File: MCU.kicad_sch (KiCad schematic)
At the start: 15 parts, among them U4 EFM32GG332, Y1 Crystal_GND23

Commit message: Added LED-s to mcu
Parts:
- added R18, R21, R22, R23, R24: 100, symbol Device:R
- added U11, U12: ~, symbol GuitarZero:LED_matrix
- C1: value 10µF -> 10u
- C1, C4: value 0.1µF -> 0.1u
- C1: value 10nF -> 10n
- C1: value 1µF -> 1u
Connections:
- net at U4.10 (PC1): now also U11.7 (C2)
- net at U4.11 (PC2): now also U11.8 (C3)
- net at U4.12 (PC3): now also U11.9 (C4)
- net at U4.13 (PC4): now also U11.10 (C5)
- net at U4.14 (PC5): now also U11.11 (C6)
- net at U4.15 (PB7): now also U11.12 (C7)
- net at U4.16 (PB8): now also R18.2
- net at U4.17 (PA8): now also R21.2
- net at U4.18 (PA9): now also R22.2
- net at U4.19 (PA10): now also R23.2
- net at U4.21 (PB11): now also R24.2
- net at U4.58 (PE9): now also U12.6 (C1)
- net at U4.59 (PE10): now also U12.7 (C2)
- net at U4.60 (PE11): now also U12.8 (C3)
- net at U4.61 (PE12): now also U12.9 (C4)
- net at U4.62 (PE13): now also U12.10 (C5)
- net at U4.63 (PE14): now also U12.11 (C6)
- net at U4.64 (PE15): now also U12.12 (C7)
- net at U4.9 (PC0): now also U11.6 (C1)
- new net: R24.1, U11.1 (R1), U12.1 (R1)
- new net: R21.1, U11.4 (R4), U12.4 (R4)
- new net: R23.1, U11.2 (R2), U12.2 (R2)
- new net: R22.1, U11.3 (R3), U12.3 (R3)
- new net: R18.1, U11.5 (R5), U12.5 (R5)
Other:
- moved on the sheet: C1

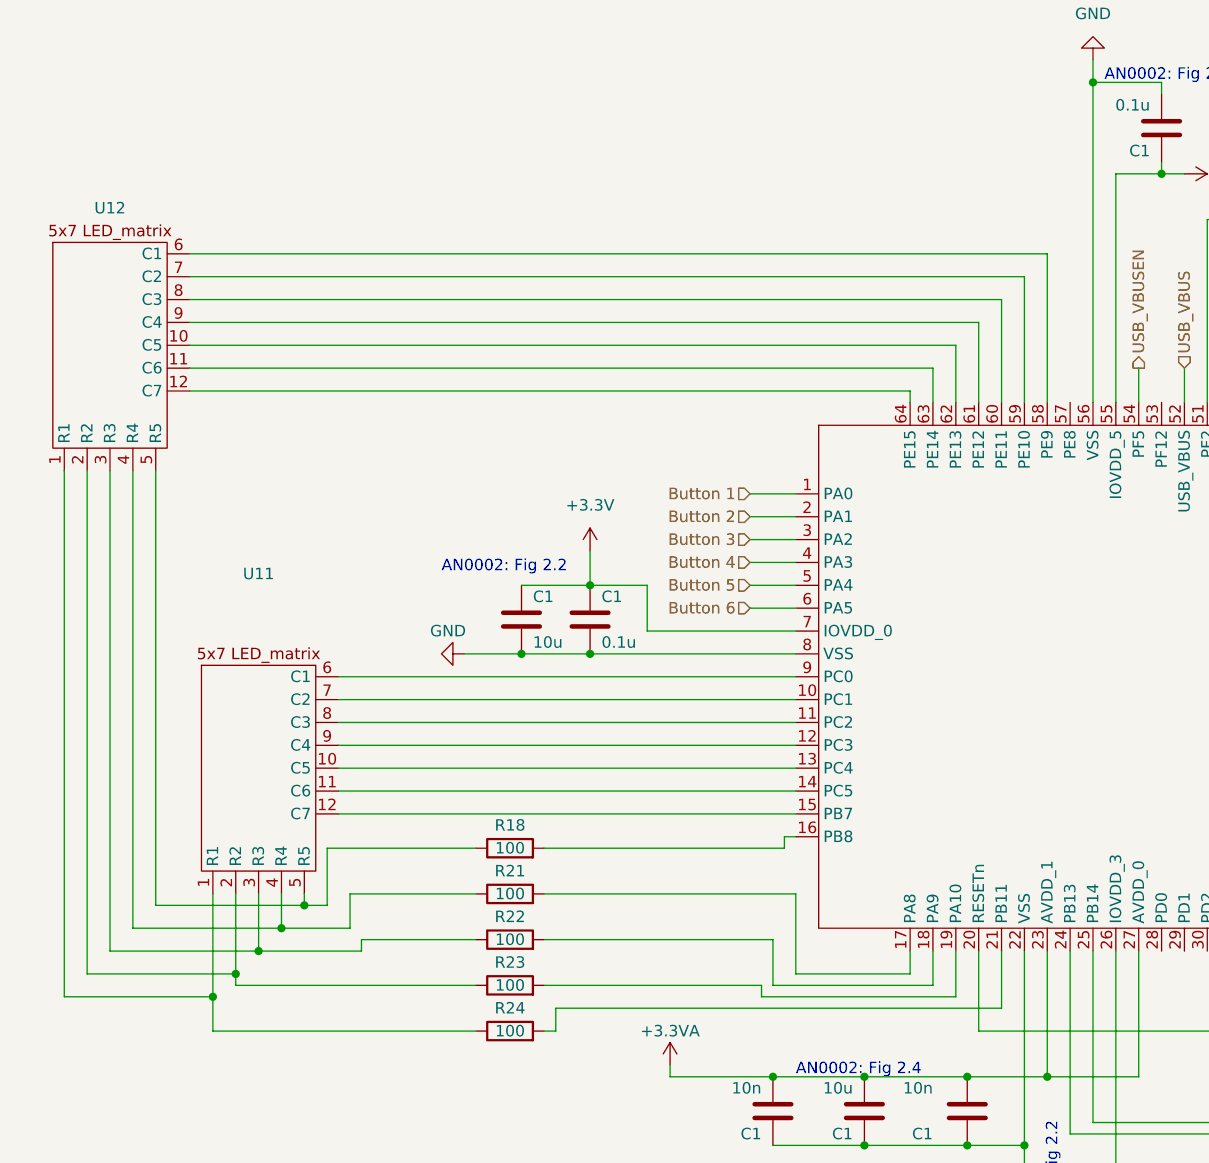
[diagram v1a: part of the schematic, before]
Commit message: Updated LEDs to match 14 pin layout
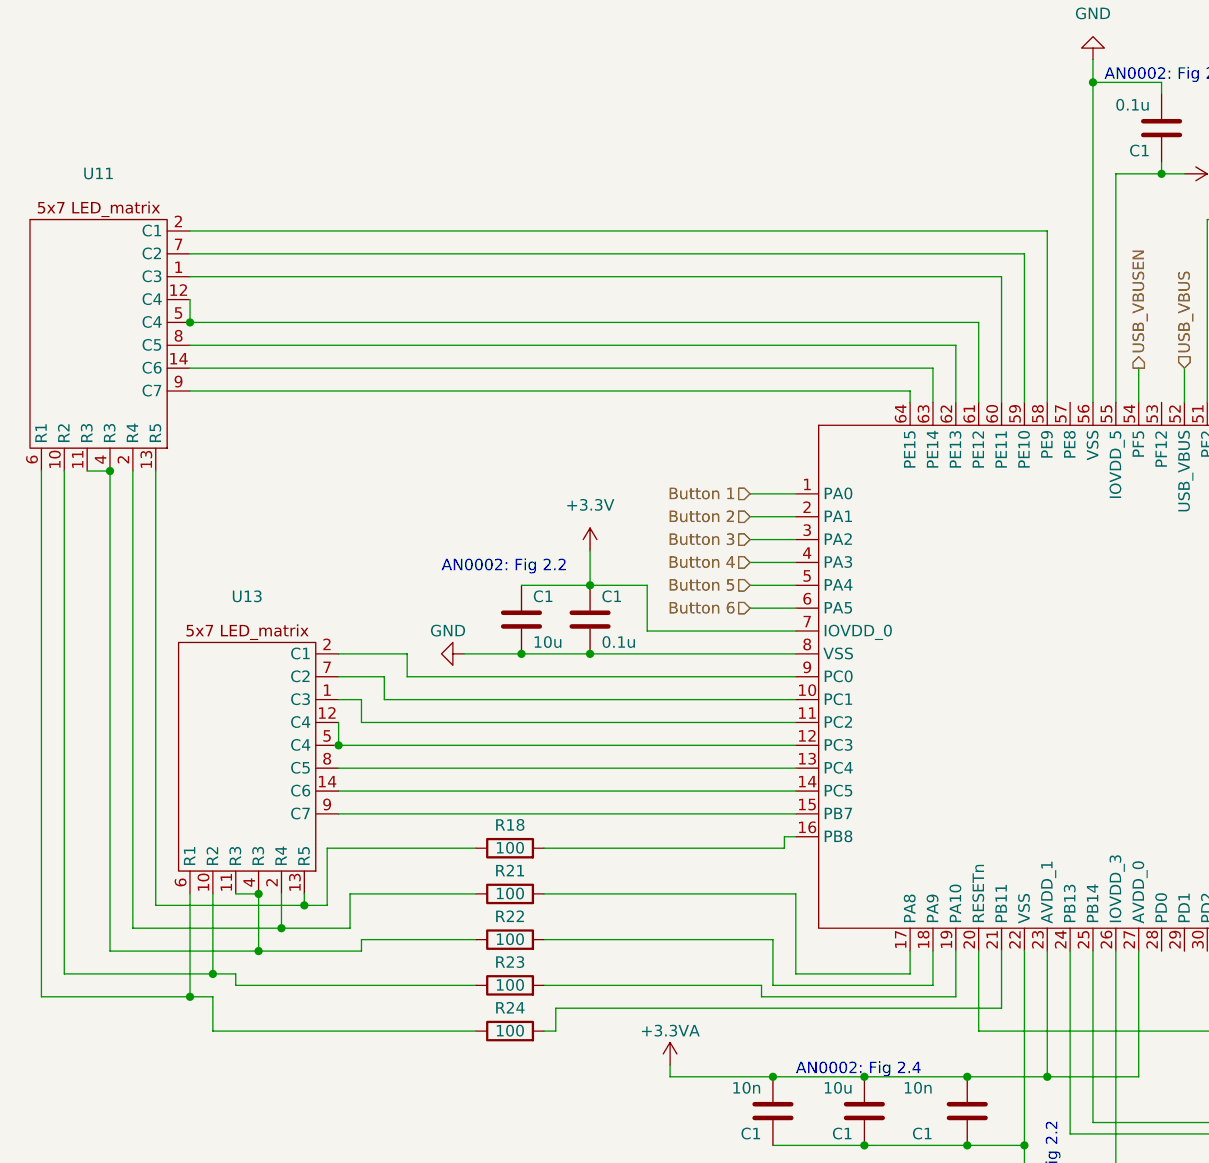
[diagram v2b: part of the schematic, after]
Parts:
- removed U12: ~, symbol GuitarZero:LED_matrix
- added U13: ~, symbol GuitarZero:LED_matrix
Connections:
- net at R24.1: now also U11.6 (R1), U13.6 (R1); no longer U11.1 (R1)
- net at R21.1: now also U11.2 (R4), U13.2 (R4); no longer U11.4 (R4)
- net at U4.62 (PE13): now also U11.8 (C5)
- net at U4.63 (PE14): now also U11.14 (C6)
- net at U4.64 (PE15): now also U11.9 (C7)
- net at U11.2 (R4): now also U4.58 (PE9); no longer R23.1
- net at R22.1: now also U11.11 (R3), U11.4 (R3), U13.11 (R3), U13.4 (R3); no longer U11.3 (R3)
- net at R18.1: now also U11.13 (R5), U13.13 (R5); no longer U11.5 (R5)
- net at U4.59 (PE10): now also U11.7 (C2)
- net at U4.60 (PE11): now also U11.1 (C3)
- net at U4.61 (PE12): now also U11.12 (C4), U11.5 (C4)
- net at U4.10 (PC1): now also U13.7 (C2); no longer U11.7 (C2)
- net at U4.11 (PC2): now also U13.1 (C3); no longer U11.8 (C3)
- net at U4.12 (PC3): now also U13.12 (C4), U13.5 (C4); no longer U11.9 (C4)
- net at U4.13 (PC4): now also U13.8 (C5); no longer U11.10 (C5)
- net at U4.14 (PC5): now also U13.14 (C6); no longer U11.11 (C6)
- net at U4.15 (PB7): now also U13.9 (C7); no longer U11.12 (C7)
- net at U4.9 (PC0): now also U13.2 (R4); no longer U11.6 (C1)
- new net: R23.1, U11.10 (R2), U13.10 (R2)

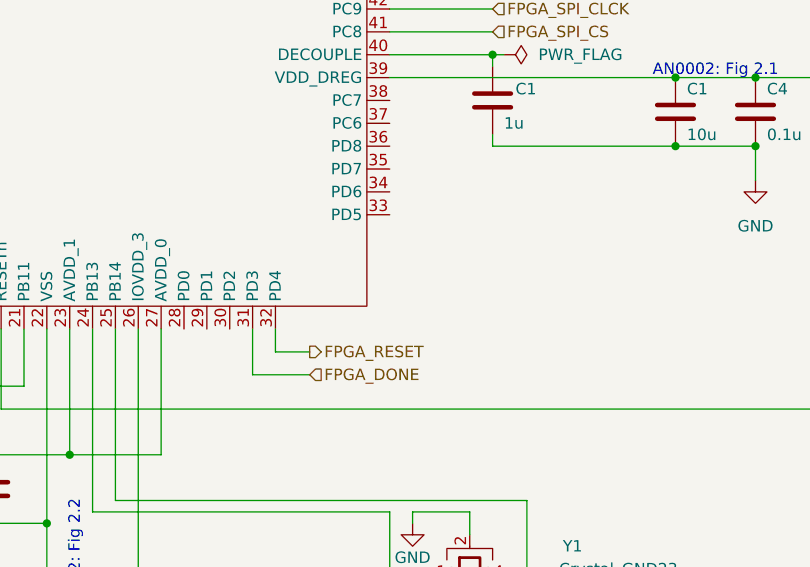
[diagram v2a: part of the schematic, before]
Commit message: move FPGA_RESET and FPGA_DONE to free US1 pins for SD-card
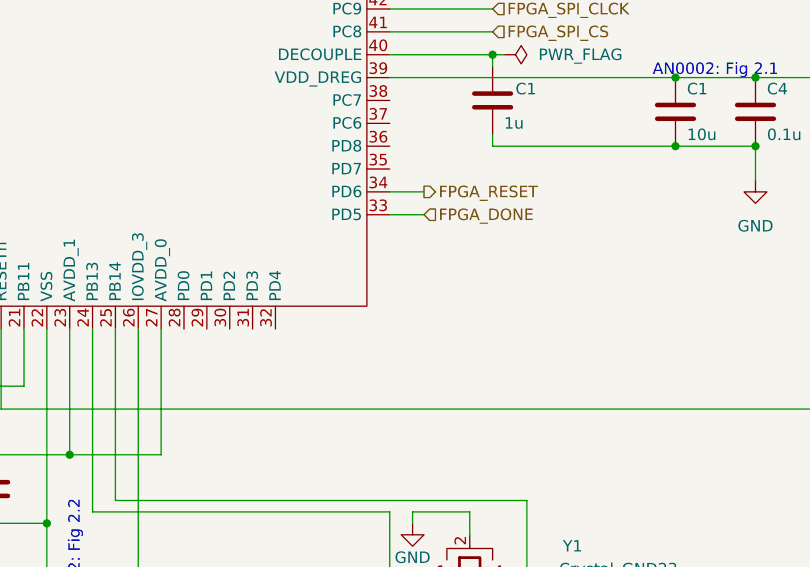
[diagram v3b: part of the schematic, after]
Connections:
- net FPGA_DONE: now also U4.33 (PD5); no longer U4.31 (PD3)
- net FPGA_RESET: now also U4.34 (PD6); no longer U4.32 (PD4)
- new net: R21.1, U11.2 (R4), U13.2 (R4)
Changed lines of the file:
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@@
+    (stroke (width 0) (type default))
+  )
+  (wire (pts (xy 162.56 111.76) (xy 166.37 111.76))
     (stroke (width 0) (type default))
   )
@@
     (stroke (width 0) (type default))
   )
-  (wire (pts (xy 153.67 129.54) (xy 147.32 129.54))
-    (stroke (width 0) (type default))
-  )
   (wire (pts (xy 31.75 62.23) (xy 111.76 62.23))
     (stroke (width 0) (type default))
   )
-  (wire (pts (xy 153.67 127) (xy 149.86 127))
-    (stroke (width 0) (type default))
-  )
   (wire (pts (xy 31.75 59.69) (xy 114.3 59.69))
     (stroke (width 0) (type default))
@@
     (stroke (width 0) (type default))
   )
-  (wire (pts (xy 147.32 129.54) (xy 147.32 124.46))
-    (stroke (width 0) (type default))
-  )
   (wire (pts (xy 31.75 54.61) (xy 119.38 54.61))
     (stroke (width 0) (type default))
   )
-  (wire (pts (xy 149.86 127) (xy 149.86 124.46))
+  (wire (pts (xy 162.56 109.22) (xy 166.37 109.22))
     (stroke (width 0) (type default))
   )
@@
     (effects (font (size 1.27 1.27)) (justify left))
   )
-  (hierarchical_label "FPGA_DONE" (shape input) (at 153.67 129.54 0) (fields_autoplaced)
+  (hierarchical_label "FPGA_DONE" (shape input) (at 166.37 111.76 0) (fields_autoplaced)
     (effects (font (size 1.27 1.27)) (justify left))
   )
@@
     (effects (font (size 1.27 1.27)) (justify left))
   )
-  (hierarchical_label "FPGA_RESET" (shape output) (at 153.67 127 0) (fields_autoplaced)
-    (effects (font (size 1.27 1.27)) (justify left))
-  )
+  (hierarchical_label "FPGA_RESET" (shape output) (at 166.37 109.22 0) (fields_autoplaced)
+    (effects (font (size 1.27 1.27)) (justify left))
+  )

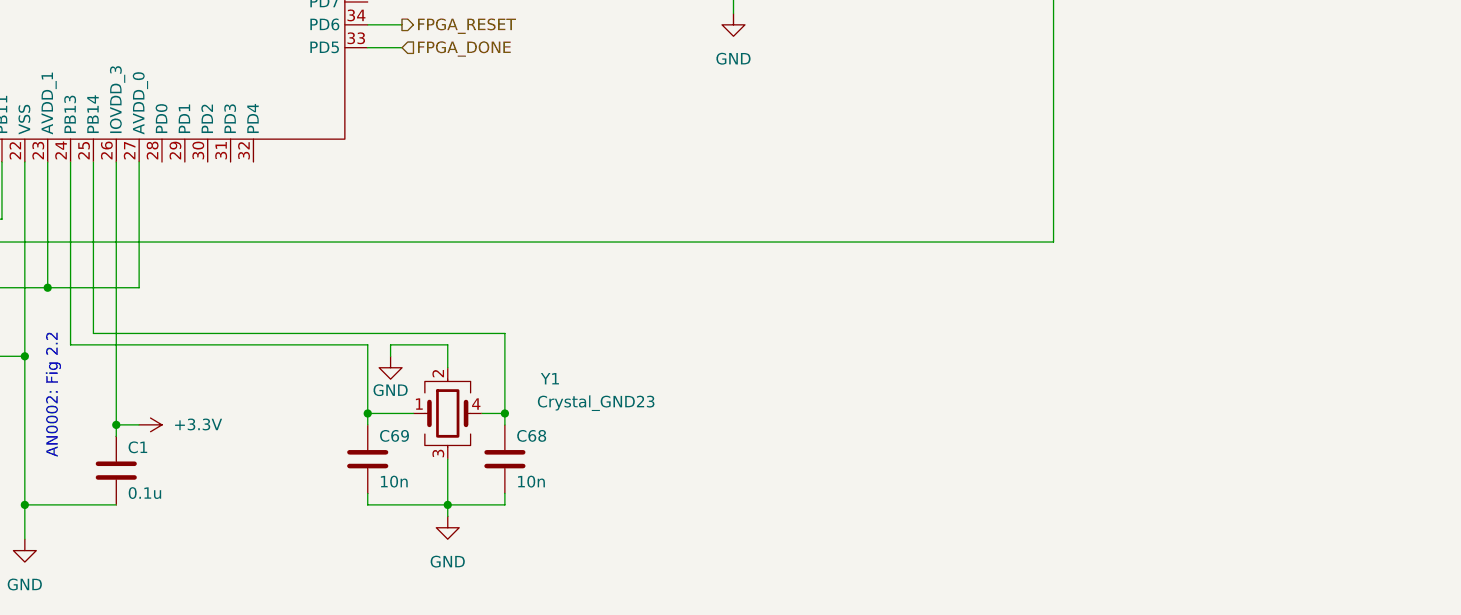
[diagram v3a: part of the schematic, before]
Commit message: add micro SD card
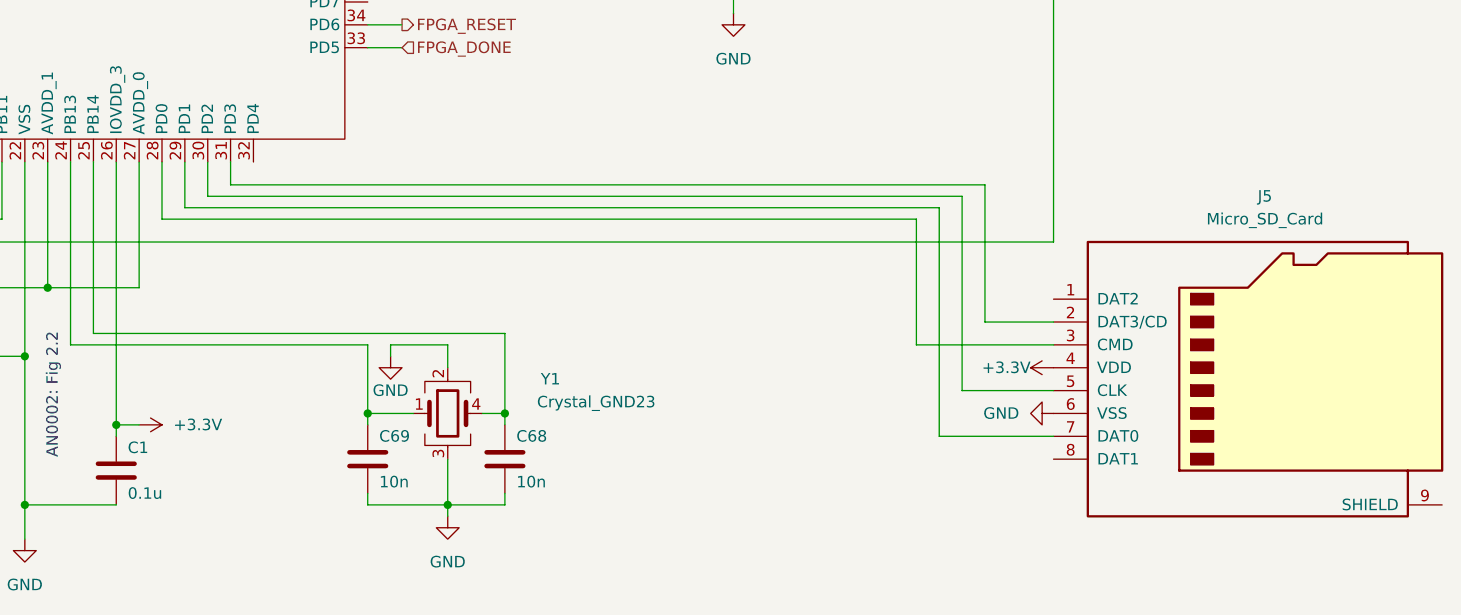
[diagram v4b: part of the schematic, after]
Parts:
- added J5: Micro_SD_Card, symbol Connector:Micro_SD_Card
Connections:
- net +3.3V: now also J5.4 (VDD)
- net GND: now also J5.6 (VSS)
- net at U4.28 (PD0): now also J5.3 (CMD)
- net at U4.29 (PD1): now also J5.7 (DAT0)
- net at U4.30 (PD2): now also J5.5 (CLK)
- net at U4.31 (PD3): now also J5.2 (DAT3/CD)
- new net: R21.1, U11.2 (R4), U13.2 (R4)
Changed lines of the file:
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@@
+    (stroke (width 0) (type default))
+  )
+  (wire (pts (xy 238.76 144.78) (xy 223.52 144.78))
+    (stroke (width 0) (type default))
+  )
+  (wire (pts (xy 228.6 149.86) (xy 228.6 128.27))
     (stroke (width 0) (type default))
   )
@@
     (stroke (width 0) (type default))
   )
+  (wire (pts (xy 231.14 127) (xy 147.32 127))
+    (stroke (width 0) (type default))
+  )
   (wire (pts (xy 171.45 144.78) (xy 171.45 147.32))
     (stroke (width 0) (type default))
   )
+  (wire (pts (xy 231.14 142.24) (xy 231.14 127))
+    (stroke (width 0) (type default))
+  )
   (wire (pts (xy 96.52 123.19) (xy 71.12 123.19))
     (stroke (width 0) (type default))
@@
     (stroke (width 0) (type default))
   )
+  (wire (pts (xy 147.32 127) (xy 147.32 124.46))
+    (stroke (width 0) (type default))
+  )
   (wire (pts (xy 149.86 48.26) (xy 149.86 63.5))
     (stroke (width 0) (type default))
@@
     (stroke (width 0) (type default))
   )
+  (wire (pts (xy 223.52 144.78) (xy 223.52 130.81))
+    (stroke (width 0) (type default))
+  )
   (wire (pts (xy 173.99 102.87) (xy 173.99 104.14))
     (stroke (width 0) (type default))
@@
     (stroke (width 0) (type default))
   )
+  (wire (pts (xy 238.76 149.86) (xy 228.6 149.86))
+    (stroke (width 0) (type default))
+  )
   (wire (pts (xy 228.6 55.88) (xy 228.6 53.34))
     (stroke (width 0) (type default))
   )
+  (wire (pts (xy 238.76 154.94) (xy 226.06 154.94))
+    (stroke (width 0) (type default))
+  )
   (wire (pts (xy 39.37 124.46) (xy 39.37 118.11))
     (stroke (width 0) (type default))
@@
     (stroke (width 0) (type default))
   )
+  (wire (pts (xy 142.24 129.54) (xy 142.24 124.46))
+    (stroke (width 0) (type default))
+  )
   (wire (pts (xy 116.84 129.54) (xy 95.25 129.54))
     (stroke (width 0) (type default))
@@
     (stroke (width 0) (type default))
   )
+  (wire (pts (xy 228.6 128.27) (xy 144.78 128.27))
+    (stroke (width 0) (type default))
+  )
   (wire (pts (xy 31.75 129.54) (xy 34.29 129.54))
     (stroke (width 0) (type default))
@@
     (stroke (width 0) (type default))
   )
+  (wire (pts (xy 139.7 130.81) (xy 139.7 124.46))
+    (stroke (width 0) (type default))
+  )
   (wire (pts (xy 173.99 104.14) (xy 194.31 104.14))
     (stroke (width 0) (type default))
@@
     (stroke (width 0) (type default))
   )
+  (wire (pts (xy 223.52 130.81) (xy 139.7 130.81))
+    (stroke (width 0) (type default))
+  )
   (wire (pts (xy 238.76 20.32) (xy 238.76 133.35))
     (stroke (width 0) (type default))
@@
     (stroke (width 0) (type default))
   )
+  (wire (pts (xy 226.06 129.54) (xy 142.24 129.54))
+    (stroke (width 0) (type default))
+  )
   (wire (pts (xy 85.09 137.16) (xy 85.09 138.43))
     (stroke (width 0) (type default))
@@
     (stroke (width 0) (type default))
   )
+  (wire (pts (xy 226.06 154.94) (xy 226.06 129.54))
+    (stroke (width 0) (type default))
+  )
   (wire (pts (xy 134.62 124.46) (xy 134.62 153.67))
     (stroke (width 0) (type default))
@@
     (stroke (width 0) (type default))
   )
+  (wire (pts (xy 238.76 142.24) (xy 231.14 142.24))
+    (stroke (width 0) (type default))
+  )
   (wire (pts (xy 137.16 59.69) (xy 137.16 63.5))
     (stroke (width 0) (type default))
@@
   )
   (wire (pts (xy 121.92 124.46) (xy 121.92 130.81))
+    (stroke (width 0) (type default))
+  )
+  (wire (pts (xy 144.78 128.27) (xy 144.78 124.46))
     (stroke (width 0) (type default))
   )
@@
         (path "/fba50eda-8593-4456-af98-ff56fd418a76/ae46c600-e32c-45ef-b9ae-c42d4bac8718"
           (reference "#PWR0102") (unit 1)
+        )
+      )
+    )
+  )
+  (symbol (lib_id "Connector:Micro_SD_Card") (at 261.62 147.32 0) (unit 1)
+    (in_bom yes) (on_board yes) (dnp no) (fields_autoplaced)
+    (property "Reference" "J5" (at 262.255 128.27 0)
+      (effects (font (size 1.27 1.27)))
+    )
+    (property "Value" "Micro_SD_Card" (at 262.255 130.81 0)
+      (effects (font (size 1.27 1.27)))
+    )
+    (property "Footprint" "" (at 290.83 139.7 0)
+      (effects (font (size 1.27 1.27)) hide)
+    )
+    (property "Datasheet" "http://katalog.we-online.de/em/datasheet/693072010801.pdf" (at 261.62 147.32 0)
+      (effects (font (size 1.27 1.27)) hide)
+    )
+    (pin "1")
+    (pin "2")
+    (pin "3")
+    (pin "4")
+    (pin "5")
+    (pin "6")
+    (pin "7")
+    (pin "8")
+    (pin "9")
+    (instances
+      (project "GuitarZero"
+        (path "/fba50eda-8593-4456-af98-ff56fd418a76/ae46c600-e32c-45ef-b9ae-c42d4bac8718"
+          (reference "J5") (unit 1)
         )
       )
@@
     )
   )
+  (symbol (lib_id "power:+3.3V") (at 238.76 147.32 90) (unit 1)
+    (in_bom yes) (on_board yes) (dnp no)
+    (property "Reference" "#PWR055" (at 242.57 147.32 0)
+      (effects (font (size 1.27 1.27)) hide)
+    )
+    (property "Value" "+3.3V" (at 236.22 147.32 90)
+      (effects (font (size 1.27 1.27)) (justify left))
+    )
+    (property "Footprint" "" (at 238.76 147.32 0)
+      (effects (font (size 1.27 1.27)) hide)
+    )
+    (property "Datasheet" "" (at 238.76 147.32 0)
+      (effects (font (size 1.27 1.27)) hide)
+    )
+    (pin "1")
+    (instances
+      (project "GuitarZero"
+        (path "/fba50eda-8593-4456-af98-ff56fd418a76/ae46c600-e32c-45ef-b9ae-c42d4bac8718"
+          (reference "#PWR055") (unit 1)
+        )
+      )
+    )
+  )
   (symbol (lib_name "LED_matrix_1") (lib_id "GuitarZero:LED_matrix") (at 40.64 113.03 180) (unit 1)
     (in_bom yes) (on_board yes) (dnp no) (fields_autoplaced)
@@
         )
       )
+    )
+  )
+  (symbol (lib_id "power:GND") (at 238.76 152.4 270) (unit 1)
+    (in_bom yes) (on_board yes) (dnp no) (fields_autoplaced)
+    (property "Reference" "#PWR054" (at 232.41 152.4 0)
+      (effects (font (size 1.27 1.27)) hide)
+    )
+    (property "Value" "GND" (at 234.95 152.4 90)
+      (effects (font (size 1.27 1.27)) (justify right))
+    )
+    (property "Footprint" "" (at 238.76 152.4 0)
+      (effects (font (size 1.27 1.27)) hide)
+    )
+    (property "Datasheet" "" (at 238.76 152.4 0)
+      (effects (font (size 1.27 1.27)) hide)
+    )
+    (pin "1")
+    (instances
+      (project "GuitarZero"
+        (path "/fba50eda-8593-4456-af98-ff56fd418a76/ae46c600-e32c-45ef-b9ae-c42d4bac8718"
+          (reference "#PWR054") (unit 1)
+        )
+      )
